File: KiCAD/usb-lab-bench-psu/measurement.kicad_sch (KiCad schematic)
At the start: 6 parts, among them J7 Conn_02x03_Top_Bottom, J8 Conn_02x03_Top_Bottom, U7 INA226

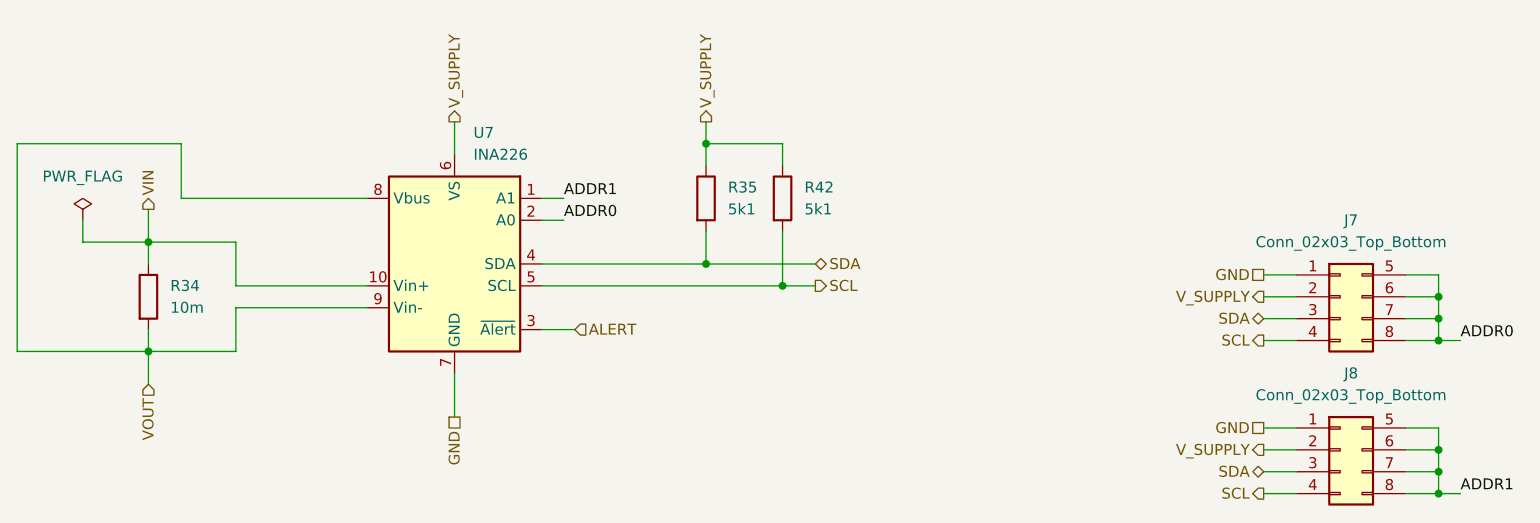
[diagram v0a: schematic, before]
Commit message: updated GND and supply nets, switched buck-boost-converter
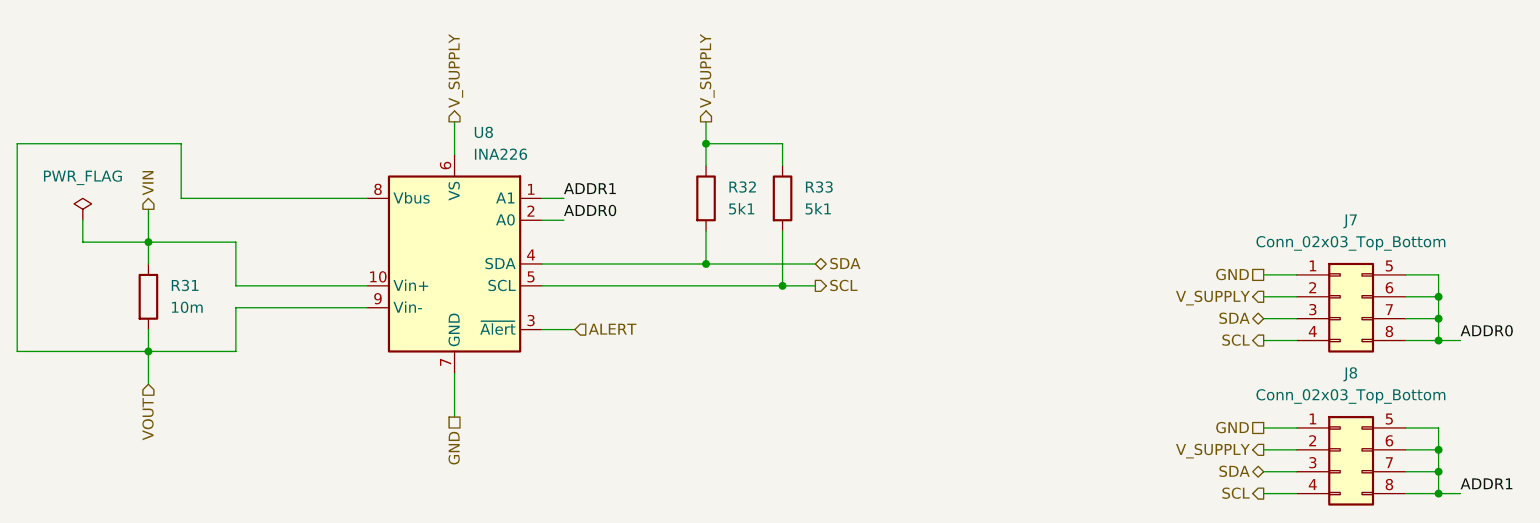
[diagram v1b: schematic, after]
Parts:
- renumbered R34 to R31, R35 to R32, R42 to R33, U7 to U8
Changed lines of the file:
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@@
 		(dnp no)
 		(fields_autoplaced yes)
-		(property "Reference" "#FLG014"
+		(property "Reference" "#FLG012"
 			(at 40.64 56.515 0)
 			(effects
@@
 			(project "usb-lab-bench-psu"
 				(path "/63928bc9-e618-488a-a687-c6d5597f31d9/b12608c4-74bb-4ec7-8be3-78c3f8a81cd8"
-					(reference "#FLG014")
+					(reference "#FLG012")
 					(unit 1)
 				)
@@
 		(dnp no)
 		(fields_autoplaced yes)
-		(property "Reference" "R34"
+		(property "Reference" "R31"
 			(at 50.8 66.0399 0)
 			(effects
@@
 			(project ""
 				(path "/63928bc9-e618-488a-a687-c6d5597f31d9/b12608c4-74bb-4ec7-8be3-78c3f8a81cd8"
-					(reference "R34")
+					(reference "R31")
 					(unit 1)
 				)
@@
 		(dnp no)
 		(fields_autoplaced yes)
-		(property "Reference" "R42"
+		(property "Reference" "R33"
 			(at 124.46 54.6099 0)
 			(effects
@@
 			(project "usb-lab-bench-psu"
 				(path "/63928bc9-e618-488a-a687-c6d5597f31d9/b12608c4-74bb-4ec7-8be3-78c3f8a81cd8"
-					(reference "R42")
+					(reference "R33")
 					(unit 1)
 				)
@@
 		(dnp no)
 		(fields_autoplaced yes)
-		(property "Reference" "R35"
+		(property "Reference" "R32"
 			(at 115.57 54.6099 0)
 			(effects
@@
 			(project ""
 				(path "/63928bc9-e618-488a-a687-c6d5597f31d9/b12608c4-74bb-4ec7-8be3-78c3f8a81cd8"
-					(reference "R35")
+					(reference "R32")
 					(unit 1)
 				)
@@
 		(dnp no)
 		(fields_autoplaced yes)
-		(property "Reference" "U7"
+		(property "Reference" "U8"
 			(at 86.0141 48.26 0)
 			(effects
@@
 			(project ""
 				(path "/63928bc9-e618-488a-a687-c6d5597f31d9/b12608c4-74bb-4ec7-8be3-78c3f8a81cd8"
-					(reference "U7")
-					(unit 1)
-				)
+					(reference "U8")
+					(unit 1)
+				)

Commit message: restructured schematics to better show individual boards
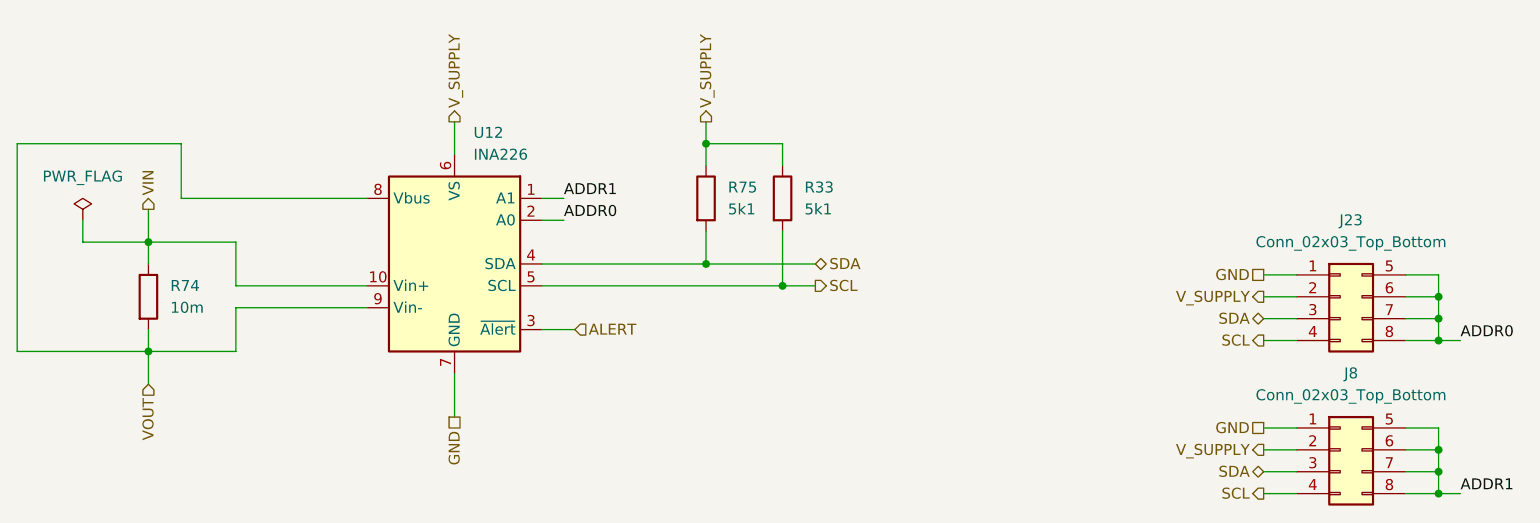
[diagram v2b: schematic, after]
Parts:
- renumbered J7 to J23, R31 to R74, R32 to R75, U8 to U12
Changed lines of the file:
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@@
 		(instances
 			(project "usb-lab-bench-psu"
-				(path "/63928bc9-e618-488a-a687-c6d5597f31d9/b12608c4-74bb-4ec7-8be3-78c3f8a81cd8"
-					(reference "J8")
+				(path "/63928bc9-e618-488a-a687-c6d5597f31d9/a793a91b-724b-4226-ba64-0dd946e3992c/1c93d33d-e5b7-4541-9c9e-21c6156d2ca5"
+					(reference "J24")
 					(unit 1)
 				)
@@
 		(dnp no)
 		(fields_autoplaced yes)
-		(property "Reference" "J7"
+		(property "Reference" "J23"
 			(at 187.96 58.42 0)
 			(effects
@@
 		)
 		(instances
-			(project ""
-				(path "/63928bc9-e618-488a-a687-c6d5597f31d9/b12608c4-74bb-4ec7-8be3-78c3f8a81cd8"
-					(reference "J7")
+			(project "usb-lab-bench-psu"
+				(path "/63928bc9-e618-488a-a687-c6d5597f31d9/a793a91b-724b-4226-ba64-0dd946e3992c/1c93d33d-e5b7-4541-9c9e-21c6156d2ca5"
+					(reference "J23")
 					(unit 1)
 				)
@@
 		(instances
 			(project "usb-lab-bench-psu"
-				(path "/63928bc9-e618-488a-a687-c6d5597f31d9/b12608c4-74bb-4ec7-8be3-78c3f8a81cd8"
-					(reference "#FLG012")
+				(path "/63928bc9-e618-488a-a687-c6d5597f31d9/a793a91b-724b-4226-ba64-0dd946e3992c/1c93d33d-e5b7-4541-9c9e-21c6156d2ca5"
+					(reference "#FLG016")
 					(unit 1)
 				)
@@
 		(dnp no)
 		(fields_autoplaced yes)
-		(property "Reference" "R31"
+		(property "Reference" "R74"
 			(at 50.8 66.0399 0)
 			(effects
@@
 		)
 		(instances
-			(project ""
-				(path "/63928bc9-e618-488a-a687-c6d5597f31d9/b12608c4-74bb-4ec7-8be3-78c3f8a81cd8"
-					(reference "R31")
+			(project "usb-lab-bench-psu"
+				(path "/63928bc9-e618-488a-a687-c6d5597f31d9/a793a91b-724b-4226-ba64-0dd946e3992c/1c93d33d-e5b7-4541-9c9e-21c6156d2ca5"
+					(reference "R74")
 					(unit 1)
 				)
@@
 		(instances
 			(project "usb-lab-bench-psu"
-				(path "/63928bc9-e618-488a-a687-c6d5597f31d9/b12608c4-74bb-4ec7-8be3-78c3f8a81cd8"
-					(reference "R33")
+				(path "/63928bc9-e618-488a-a687-c6d5597f31d9/a793a91b-724b-4226-ba64-0dd946e3992c/1c93d33d-e5b7-4541-9c9e-21c6156d2ca5"
+					(reference "R76")
 					(unit 1)
 				)
@@
 		(dnp no)
 		(fields_autoplaced yes)
-		(property "Reference" "R32"
+		(property "Reference" "R75"
 			(at 115.57 54.6099 0)
 			(effects
@@
 		)
 		(instances
-			(project ""
-				(path "/63928bc9-e618-488a-a687-c6d5597f31d9/b12608c4-74bb-4ec7-8be3-78c3f8a81cd8"
-					(reference "R32")
+			(project "usb-lab-bench-psu"
+				(path "/63928bc9-e618-488a-a687-c6d5597f31d9/a793a91b-724b-4226-ba64-0dd946e3992c/1c93d33d-e5b7-4541-9c9e-21c6156d2ca5"
+					(reference "R75")
 					(unit 1)
 				)
@@
 		(dnp no)
 		(fields_autoplaced yes)
-		(property "Reference" "U8"
+		(property "Reference" "U12"
 			(at 86.0141 48.26 0)
 			(effects
@@
 		)
 		(instances
-			(project ""
-				(path "/63928bc9-e618-488a-a687-c6d5597f31d9/b12608c4-74bb-4ec7-8be3-78c3f8a81cd8"
-					(reference "U8")
-					(unit 1)
-				)
+			(project "usb-lab-bench-psu"
+				(path "/63928bc9-e618-488a-a687-c6d5597f31d9/a793a91b-724b-4226-ba64-0dd946e3992c/1c93d33d-e5b7-4541-9c9e-21c6156d2ca5"
+					(reference "U12")
+					(unit 1)
+				)

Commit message: updated spi for display
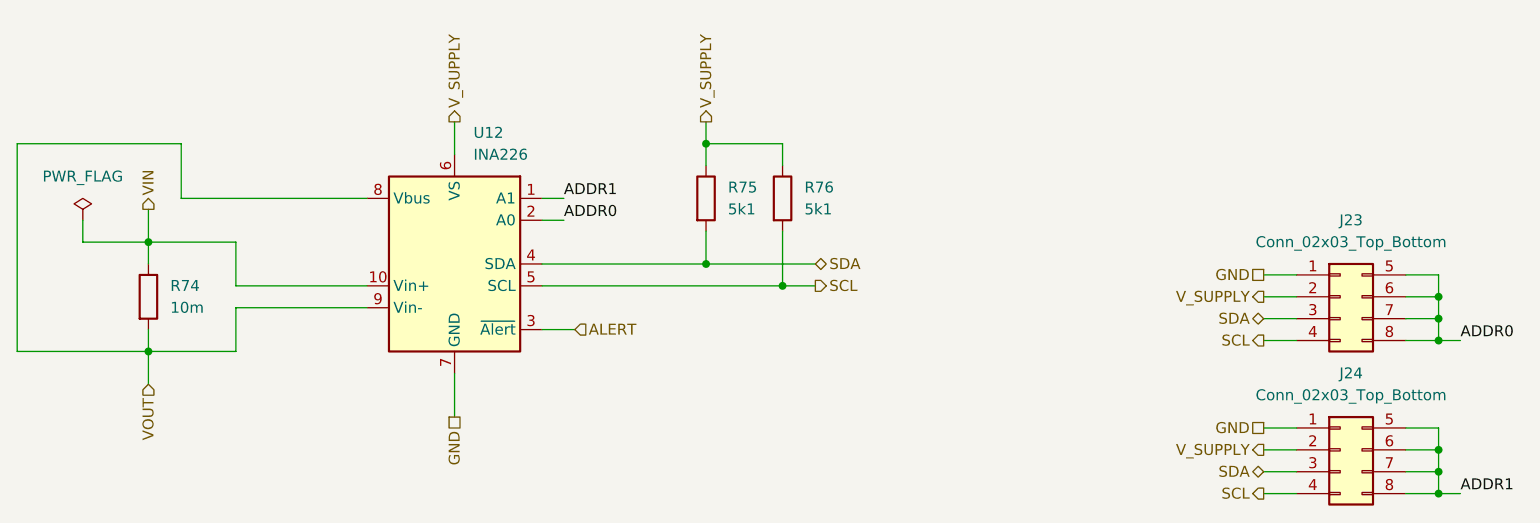
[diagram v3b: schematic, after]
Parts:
- renumbered J8 to J24, R33 to R76
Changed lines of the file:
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@@
 		(dnp no)
 		(fields_autoplaced yes)
-		(property "Reference" "J8"
+		(property "Reference" "J24"
 			(at 187.96 76.2 0)
 			(effects
@@
 		(dnp no)
 		(fields_autoplaced yes)
-		(property "Reference" "#FLG012"
+		(property "Reference" "#FLG016"
 			(at 40.64 56.515 0)
 			(effects
@@
 		(dnp no)
 		(fields_autoplaced yes)
-		(property "Reference" "R33"
+		(property "Reference" "R76"
 			(at 124.46 54.6099 0)
 			(effects

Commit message: added current limiting circuit for USB PD sink, added 2nd buck converter
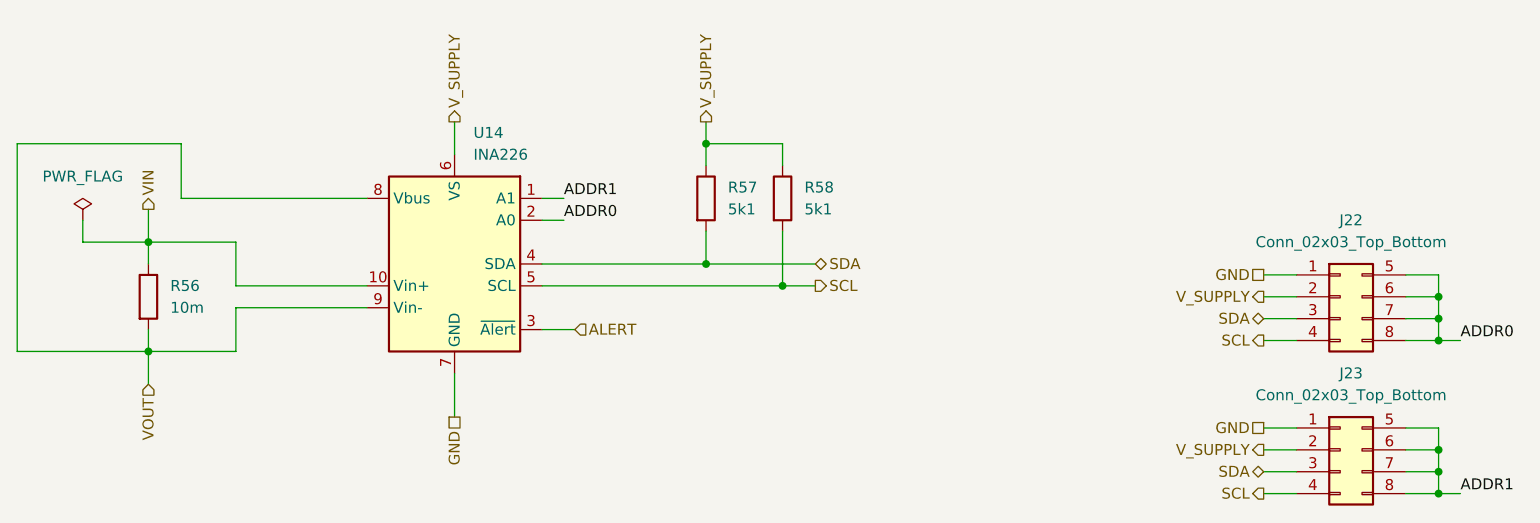
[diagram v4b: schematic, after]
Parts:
- renumbered J23 to J22, J24 to J23, R74 to R56, R75 to R57, R76 to R58, U12 to U14
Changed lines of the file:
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@@
 (kicad_sch
-	(version 20231120)
+	(version 20250114)
 	(generator "eeschema")
-	(generator_version "8.0")
+	(generator_version "9.0")
 	(paper "A4")
 	(junction
@@
 		(dnp no)
 		(fields_autoplaced yes)
-		(property "Reference" "J24"
+		(property "Reference" "J23"
 			(at 187.96 76.2 0)
 			(effects
@@
 			(project "usb-lab-bench-psu"
 				(path "/63928bc9-e618-488a-a687-c6d5597f31d9/a793a91b-724b-4226-ba64-0dd946e3992c/1c93d33d-e5b7-4541-9c9e-21c6156d2ca5"
-					(reference "J24")
+					(reference "J23")
 					(unit 1)
 				)
@@
 		(dnp no)
 		(fields_autoplaced yes)
-		(property "Reference" "J23"
+		(property "Reference" "J22"
 			(at 187.96 58.42 0)
 			(effects
@@
 			(project "usb-lab-bench-psu"
 				(path "/63928bc9-e618-488a-a687-c6d5597f31d9/a793a91b-724b-4226-ba64-0dd946e3992c/1c93d33d-e5b7-4541-9c9e-21c6156d2ca5"
-					(reference "J23")
+					(reference "J22")
 					(unit 1)
 				)
@@
 		(dnp no)
 		(fields_autoplaced yes)
-		(property "Reference" "#FLG016"
+		(property "Reference" "#FLG015"
 			(at 40.64 56.515 0)
 			(effects
@@
 			(project "usb-lab-bench-psu"
 				(path "/63928bc9-e618-488a-a687-c6d5597f31d9/a793a91b-724b-4226-ba64-0dd946e3992c/1c93d33d-e5b7-4541-9c9e-21c6156d2ca5"
-					(reference "#FLG016")
+					(reference "#FLG015")
 					(unit 1)
 				)
@@
 		(dnp no)
 		(fields_autoplaced yes)
-		(property "Reference" "R74"
+		(property "Reference" "R56"
 			(at 50.8 66.0399 0)
 			(effects
@@
 			(project "usb-lab-bench-psu"
 				(path "/63928bc9-e618-488a-a687-c6d5597f31d9/a793a91b-724b-4226-ba64-0dd946e3992c/1c93d33d-e5b7-4541-9c9e-21c6156d2ca5"
-					(reference "R74")
+					(reference "R56")
 					(unit 1)
 				)
@@
 		(dnp no)
 		(fields_autoplaced yes)
-		(property "Reference" "R76"
+		(property "Reference" "R58"
 			(at 124.46 54.6099 0)
 			(effects
@@
 			(project "usb-lab-bench-psu"
 				(path "/63928bc9-e618-488a-a687-c6d5597f31d9/a793a91b-724b-4226-ba64-0dd946e3992c/1c93d33d-e5b7-4541-9c9e-21c6156d2ca5"
-					(reference "R76")
+					(reference "R58")
 					(unit 1)
 				)
@@
 		(dnp no)
 		(fields_autoplaced yes)
-		(property "Reference" "R75"
+		(property "Reference" "R57"
 			(at 115.57 54.6099 0)
 			(effects
@@
 			(project "usb-lab-bench-psu"
 				(path "/63928bc9-e618-488a-a687-c6d5597f31d9/a793a91b-724b-4226-ba64-0dd946e3992c/1c93d33d-e5b7-4541-9c9e-21c6156d2ca5"
-					(reference "R75")
+					(reference "R57")
 					(unit 1)
 				)
@@
 		(dnp no)
 		(fields_autoplaced yes)
-		(property "Reference" "U12"
+		(property "Reference" "U14"
 			(at 86.0141 48.26 0)
 			(effects
@@
 			(project "usb-lab-bench-psu"
 				(path "/63928bc9-e618-488a-a687-c6d5597f31d9/a793a91b-724b-4226-ba64-0dd946e3992c/1c93d33d-e5b7-4541-9c9e-21c6156d2ca5"
-					(reference "U12")
+					(reference "U14")
 					(unit 1)
 				)

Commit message: Fixed label directions
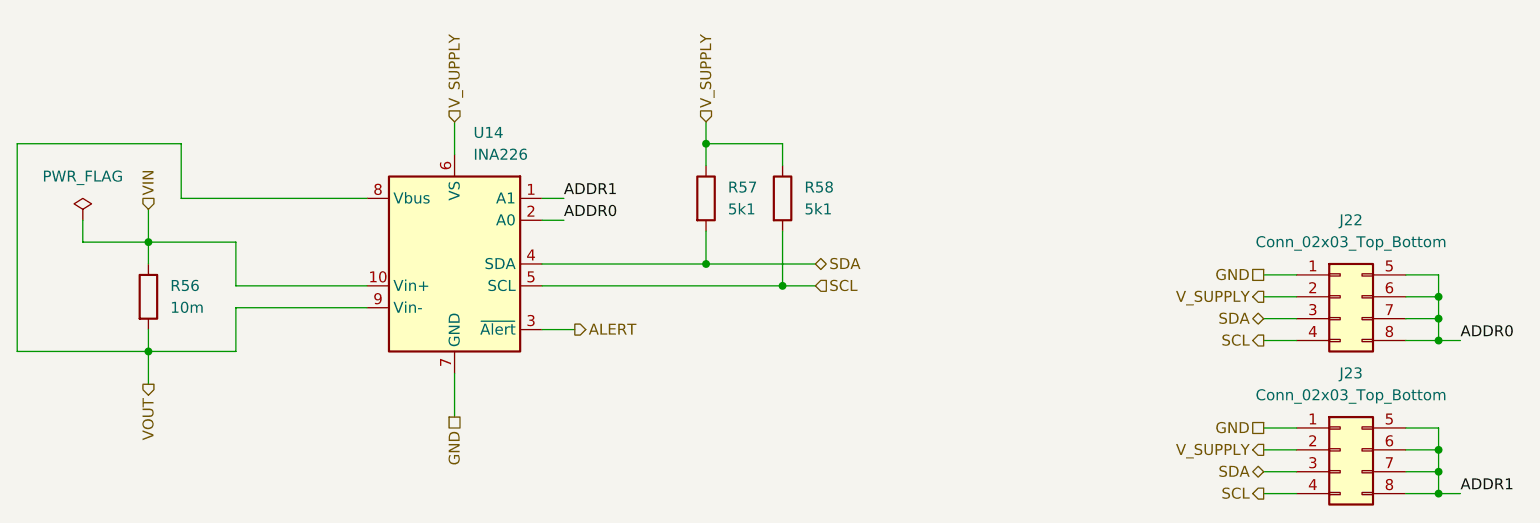
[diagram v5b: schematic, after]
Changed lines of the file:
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@@
 	)
 	(hierarchical_label "V_SUPPLY"
-		(shape output)
+		(shape input)
 		(at 113.03 46.99 90)
 		(effects
@@
 	)
 	(hierarchical_label "VIN"
-		(shape output)
+		(shape input)
 		(at 48.26 57.15 90)
 		(effects
@@
 	)
 	(hierarchical_label "SCL"
-		(shape output)
+		(shape input)
 		(at 125.73 66.04 0)
 		(effects
@@
 	)
 	(hierarchical_label "ALERT"
-		(shape input)
+		(shape output)
 		(at 97.79 71.12 0)
 		(effects
@@
 	)
 	(hierarchical_label "VOUT"
-		(shape input)
+		(shape output)
 		(at 48.26 77.47 270)
 		(effects
@@
 	)
 	(hierarchical_label "V_SUPPLY"
-		(shape output)
+		(shape input)
 		(at 83.82 46.99 90)
 		(effects
